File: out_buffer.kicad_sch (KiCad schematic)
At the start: 5 parts, among them U2 SN74LVC3G34DCT

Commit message: Completed Schematic
Completed Schematic Draft
- Includes careful pin mapping to avoid conflicts with other firmwares
- Roughed out LCB layout high speed traces, and FMC breakouts.

Layout and BOM are still WIP
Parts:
- U2: symbol 0local:SN74LVC3G34DCT -> evr-fmc:SN74LVC3G34DCT
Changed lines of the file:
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@@
 	)
 	(symbol
-		(lib_id "0local:SN74LVC3G34DCT")
+		(lib_id "evr-fmc:SN74LVC3G34DCT")
 		(at 148.59 97.79 0)
 		(unit 1)

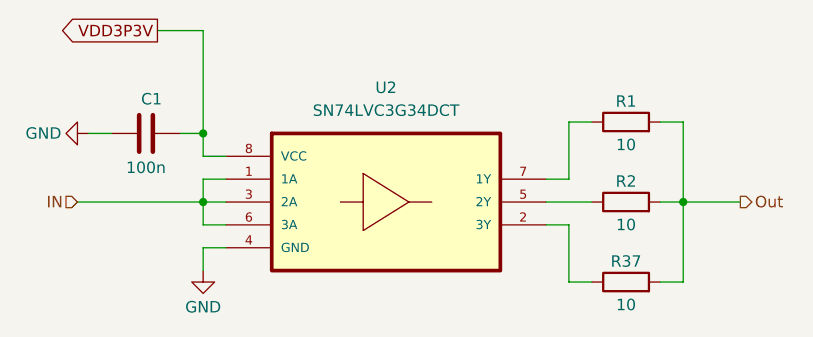
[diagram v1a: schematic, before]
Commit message: Updated Schematic and continued layout work
schematic:
- Added 0ohm resistor in power section
- Added pull up and down to digital lines to define powerup behavior
- Added some power filter between jitter cleaner IC's

layout:
-Overall Still WIP
-defined all needed fmc pins
-started layout of critical clock signals and connector locations.
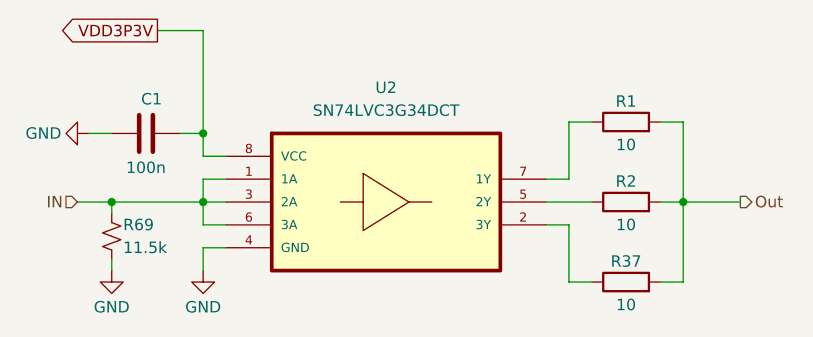
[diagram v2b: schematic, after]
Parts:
- added R69: 11.5k, Resistor_SMD:R_0603_1608Metric, symbol Device:R_Small_US
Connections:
- net GND: now also R69.2
- net IN: now also R69.1

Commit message: Finalized Schematic and Updated Layout
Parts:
- R1, R2, R37: footprint Resistor_SMD:R_0805_2012Metric -> Resistor_SMD:R_0603_1608Metric
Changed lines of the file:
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@@
 			)
 		)
-		(property "Footprint" "Resistor_SMD:R_0805_2012Metric"
+		(property "Footprint" "Resistor_SMD:R_0603_1608Metric"
 			(at 175.26 90.678 90)
 			(effects
@@
 			)
 		)
-		(property "Footprint" "Resistor_SMD:R_0805_2012Metric"
+		(property "Footprint" "Resistor_SMD:R_0603_1608Metric"
 			(at 175.26 108.458 90)
 			(effects
@@
 			)
 		)
-		(property "Footprint" "Resistor_SMD:R_0805_2012Metric"
+		(property "Footprint" "Resistor_SMD:R_0603_1608Metric"
 			(at 175.26 99.568 90)
 			(effects

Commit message: Final Draft - Ready to Review
Things to do:
Round diff traces before generting fabrication files
Change name of project to 'trigger output fmc'
Align this with recent updates to fmc-template

Updates:
- Cleaned up BOM
- Arranged silkscreen and fab layers
- Shortened power traces from LDOs to Jitter Cleaner IC
- Fixed traces/planes with sharp corners
- Straightened out all MMCX Test Ports
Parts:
- C1: Manufacturer (none) -> Samsung
- R1, R2, R37: Manufacturer (none) -> Yageo
- U2: Manufacturer (none) -> Texas Instruments
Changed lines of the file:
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@@
 			)
 		)
-		(property "Description" "10 Ohms ±1% 0.125W, 1/8W Chip Resistor 0805 (2012 Metric) Moisture Resistant Thick Film"
+		(property "Description" "RES 10 OHM 1% 1/8W 0805"
 			(at 175.26 88.9 0)
 			(effects
@@
 		)
 		(property "MPN" "RC0805FR-1010RL"
+			(at 175.26 88.9 90)
+			(effects
+				(font
+					(size 1.27 1.27)
+				)
+				(hide yes)
+			)
+		)
+		(property "Manufacturer" "Yageo"
 			(at 175.26 88.9 90)
 			(effects
@@
 			)
 		)
-		(property "Description" "0.1 µF ±10% 50V Ceramic Capacitor X7R 0603"
+		(property "Description" "CAP CER 0.1UF 50V X7R 0603"
 			(at 121.92 90.17 0)
 			(effects
@@
 		)
 		(property "MPN" "CL10B104KB8NNWC"
+			(at 121.92 90.17 90)
+			(effects
+				(font
+					(size 1.27 1.27)
+				)
+				(hide yes)
+			)
+		)
+		(property "Manufacturer" "Samsung"
 			(at 121.92 90.17 90)
 			(effects
@@
 			)
 		)
+		(property "Manufacturer" "Texas Instruments"
+			(at 148.59 97.79 0)
+			(effects
+				(font
+					(size 1.27 1.27)
+				)
+				(hide yes)
+			)
+		)
 		(pin "8"
 		)
@@
 			)
 		)
-		(property "Description" "10 Ohms ±1% 0.125W, 1/8W Chip Resistor 0805 (2012 Metric) Moisture Resistant Thick Film"
+		(property "Description" "RES 10 OHM 1% 1/8W 0805"
 			(at 175.26 106.68 0)
 			(effects
@@
 		)
 		(property "MPN" "RC0805FR-1010RL"
+			(at 175.26 106.68 90)
+			(effects
+				(font
+					(size 1.27 1.27)
+				)
+				(hide yes)
+			)
+		)
+		(property "Manufacturer" "Yageo"
 			(at 175.26 106.68 90)
 			(effects
@@
 			)
 		)
-		(property "Description" "10 Ohms ±1% 0.125W, 1/8W Chip Resistor 0805 (2012 Metric) Moisture Resistant Thick Film"
+		(property "Description" "RES 10 OHM 1% 1/8W 0805"
 			(at 175.26 97.79 0)
 			(effects
@@
 			(at 175.26 97.79 90)
 			(effects
+				(font
+					(size 1.27 1.27)
+				)
+				(hide yes)
+			)
+		)
+		(property "Manufacturer" "Yageo"
+			(at 175.26 97.79 90)
+			(effects

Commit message: Final Draft - Ready for review
Updates:
- Changed area behind FMC connector to match the new Osprey FMC template
  - This includes a new 12V LED, more robust power input traces, arranged elements for readability.

Things to do:
Round diff traces before generating fabrication files
Change name of project to 'trigger output fmc'
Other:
- title: FMC Template -> Trigger Output FMC
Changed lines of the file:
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@@
 	(paper "A4")
 	(title_block
-		(title "FMC Template")
-		(date "2026-01-26")
+		(title "Trigger Output FMC")
+		(date "2026-05-07")
 		(rev "1.0")
 		(company "SPDX-FileCopyrightText: 2025 Osprey DCS")
@@
 			)
 		)
-		(property "Datasheet" ""
+		(property "Datasheet" "~"
 			(at 175.26 88.9 0)
 			(effects
@@
 			)
 		)
-		(property "Datasheet" ""
+		(property "Datasheet" "~"
 			(at 121.92 90.17 0)
 			(effects
@@
 			)
 		)
-		(property "Datasheet" ""
+		(property "Datasheet" "~"
 			(at 175.26 106.68 0)
 			(effects
@@
 			)
 		)
-		(property "Datasheet" ""
+		(property "Datasheet" "~"
 			(at 175.26 97.79 0)
 			(effects

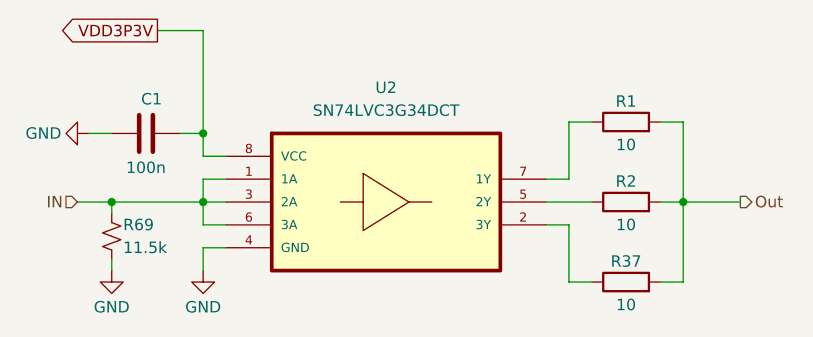
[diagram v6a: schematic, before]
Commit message: Changed Trigger Outputs Topology
- Changed to a comp to digital TX design
- Added power section to support this change
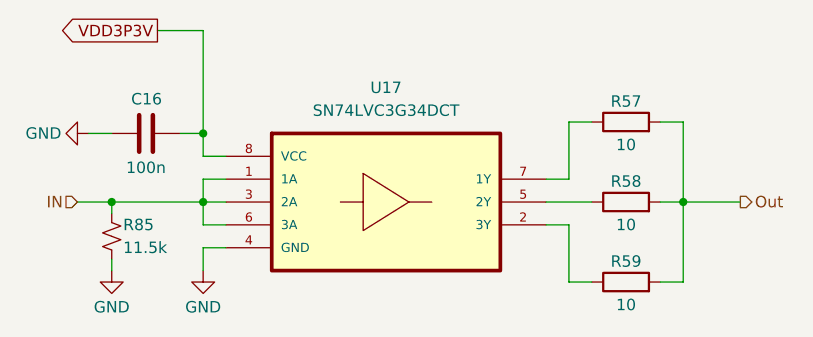
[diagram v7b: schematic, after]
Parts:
- renumbered C1 to C16, R1 to R57, R2 to R58, R37 to R59, R69 to R85, U2 to U17
